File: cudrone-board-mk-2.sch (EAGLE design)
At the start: 170 parts, among them U1 EDISON_CONNECTOR_FULLMOUNTING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, U10 A2235-H, U11 FTS31XS-U, U12 BNO055, U13 DSPIC33EP512MU810-X_PF, U2 FTS31XS-U, U4 TPS62065, U5 USD-SOCKETNEW, U6 TXB0108, U8 PCA9306, U9 PCA9306

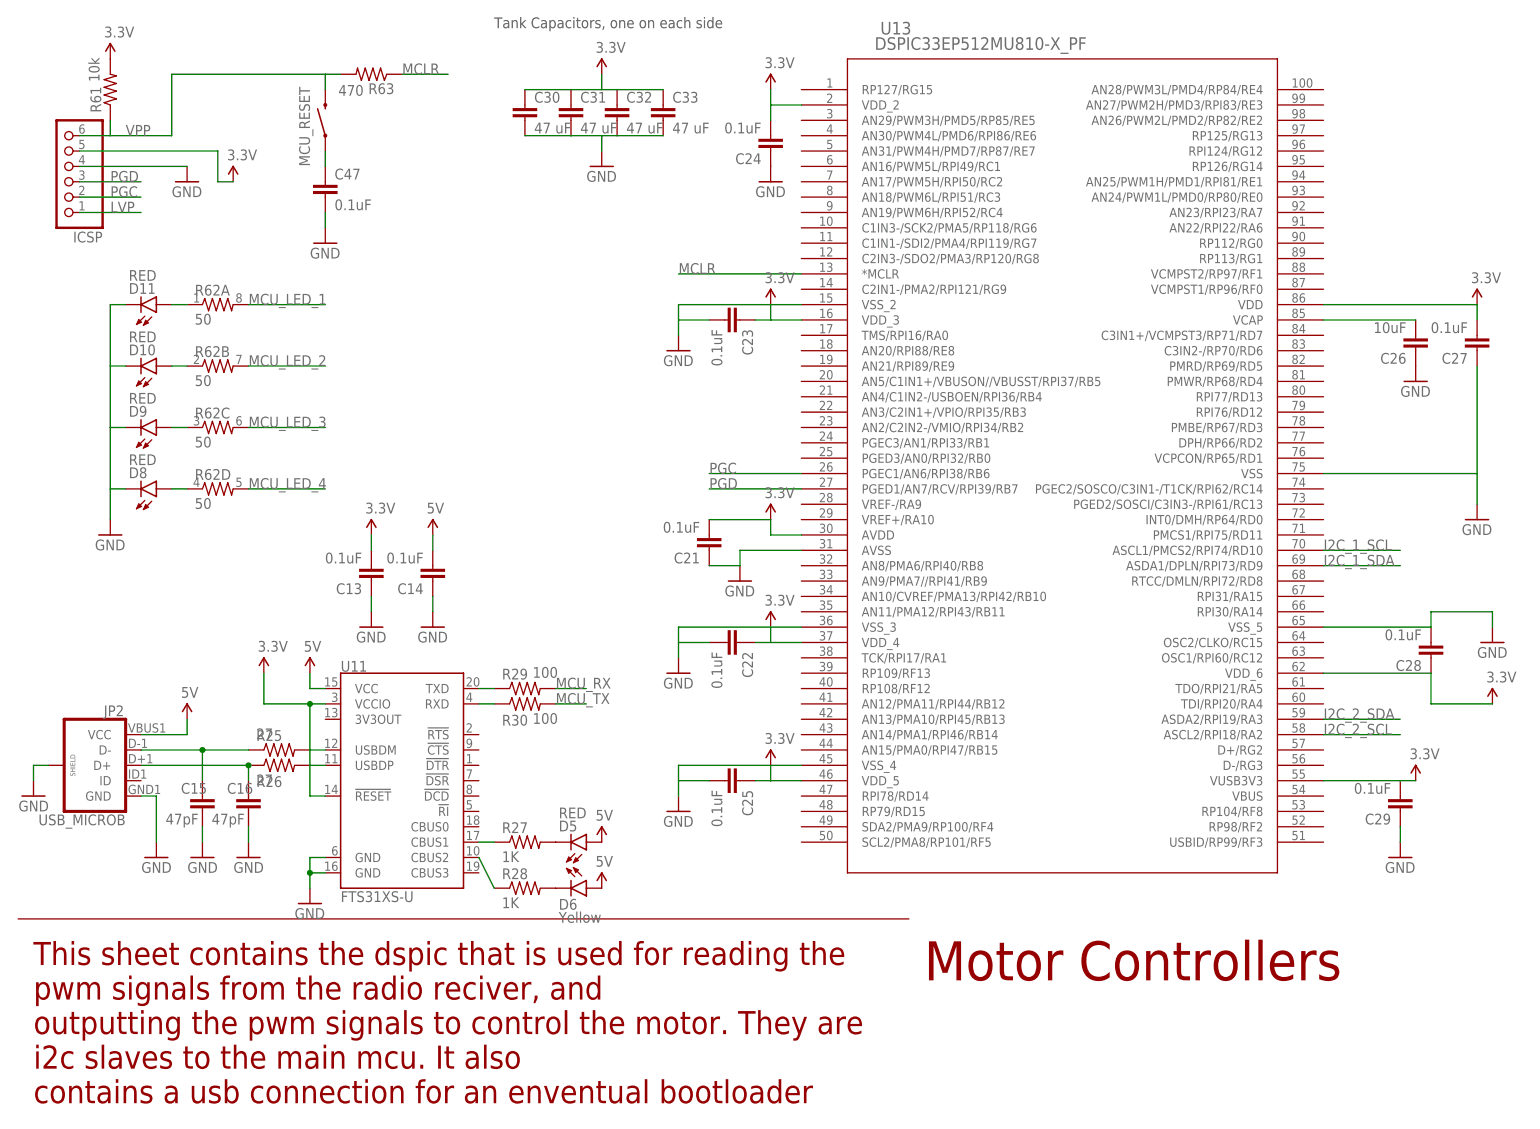
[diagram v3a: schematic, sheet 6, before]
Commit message: Added resinator to mcu
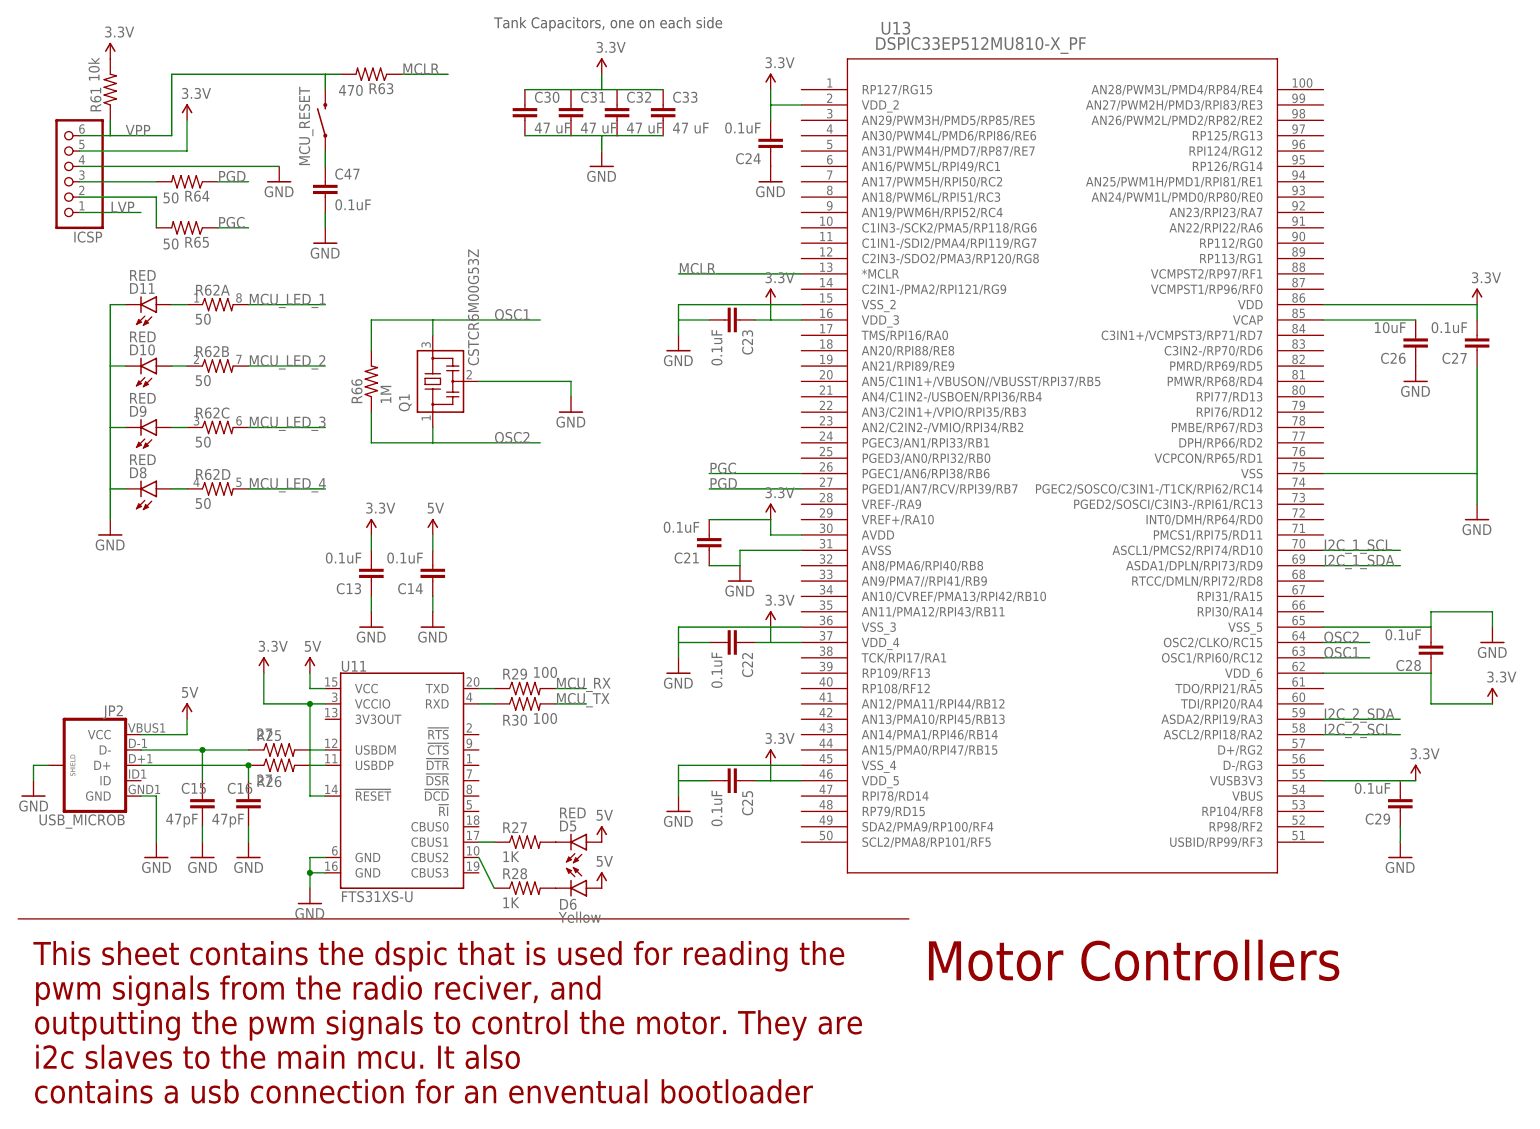
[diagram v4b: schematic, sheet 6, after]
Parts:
- added Q1: CSTCR6M00G53Z, murata-filter:CSTCR6M00G53Z
- added R64, R65: 50, SparkFun-Resistors:27OHM1/10W1%(0603)
- added R66: 1M, SparkFun-Resistors:27OHM1/10W1%(0603)
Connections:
- new net N$46: ICSP.3, R64.2
- new net N$47: ICSP.2, R65.2
- new net OSC1: Q1.3, R66.2, U13.OSC1/RPI60/RC12
- new net OSC2: Q1.1, R66.1, U13.OSC2/CLKO/RC15
- net GND: now also Q1.2
- net PGC: now also R65.1; no longer ICSP.2
- net PGD: now also R64.1; no longer ICSP.3
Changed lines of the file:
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@@
 <part name="MCU_RESET" library="SparkFun-Electromechanical" deviceset="SWITCH-MOMENTARY-2" device=""/>
 <part name="GND83" library="SparkFun-Aesthetics" deviceset="GND" device=""/>
+<part name="R64" library="SparkFun-Resistors" deviceset="27OHM1/10W1%(0603)" device="" value="50"/>
+<part name="R65" library="SparkFun-Resistors" deviceset="27OHM1/10W1%(0603)" device="" value="50"/>
+<part name="Q1" library="murata-filter" deviceset="CSTCR" device="" technology="6M00G53Z"/>
+<part name="GND84" library="SparkFun-Aesthetics" deviceset="GND" device=""/>
+<part name="R66" library="SparkFun-Resistors" deviceset="27OHM1/10W1%(0603)" device="" value="1M"/>
 </parts>
 <sheets>
@@
 <instance part="GND56" gate="1" x="109.22" y="129.54"/>
 <instance part="ICSP" gate="A" x="7.62" y="160.02" rot="R180"/>
-<instance part="GND57" gate="1" x="27.94" y="157.48"/>
-<instance part="SUPPLY100" gate="G$1" x="35.56" y="157.48"/>
+<instance part="GND57" gate="1" x="43.18" y="157.48"/>
+<instance part="SUPPLY100" gate="G$1" x="27.94" y="167.64"/>
 <instance part="R61" gate="G$1" x="15.24" y="172.72" smashed="yes" rot="R90">
 <attribute name="NAME" x="13.7414" y="168.91" size="1.778" layer="95" rot="R90"/>
@@
 </instance>
 <instance part="GND83" gate="1" x="50.8" y="147.32"/>
+<instance part="R64" gate="G$1" x="27.94" y="157.48" smashed="yes" rot="R180">
+<attribute name="NAME" x="31.75" y="155.9814" size="1.778" layer="95" rot="R180"/>
+<attribute name="VALUE" x="26.67" y="155.702" size="1.778" layer="96" rot="R180"/>
+</instance>
+<instance part="R65" gate="G$1" x="27.94" y="149.86" smashed="yes" rot="R180">
+<attribute name="NAME" x="31.75" y="148.3614" size="1.778" layer="95" rot="R180"/>
+<attribute name="VALUE" x="26.67" y="148.082" size="1.778" layer="96" rot="R180"/>
+</instance>
+<instance part="Q1" gate="G$1" x="68.58" y="124.46" rot="R90"/>
+<instance part="GND84" gate="1" x="91.44" y="119.38"/>
+<instance part="R66" gate="G$1" x="58.42" y="124.46" smashed="yes" rot="R90">
+<attribute name="NAME" x="56.9214" y="120.65" size="1.778" layer="95" rot="R90"/>
+<attribute name="VALUE" x="61.722" y="120.65" size="1.778" layer="96" rot="R90"/>
+</instance>
 </instances>
 <busses>
@@
 <pinref part="ICSP" gate="A" pin="4"/>
 <pinref part="GND57" gate="1" pin="GND"/>
-<wire x1="10.16" y1="160.02" x2="27.94" y2="160.02" width="0.1524" layer="91"/>
+<wire x1="10.16" y1="160.02" x2="43.18" y2="160.02" width="0.1524" layer="91"/>
 </segment>
 <segment>
@@
 <wire x1="50.8" y1="149.86" x2="50.8" y2="152.4" width="0.1524" layer="91"/>
 </segment>
+<segment>
+<pinref part="Q1" gate="G$1" pin="2"/>
+<wire x1="76.2" y1="124.46" x2="91.44" y2="124.46" width="0.1524" layer="91"/>
+<pinref part="GND84" gate="1" pin="GND"/>
+<wire x1="91.44" y1="124.46" x2="91.44" y2="121.92" width="0.1524" layer="91"/>
+</segment>
 </net>
 <net name="5V" class="0">
@@
 <segment>
 <pinref part="ICSP" gate="A" pin="5"/>
-<wire x1="10.16" y1="162.56" x2="33.02" y2="162.56" width="0.1524" layer="91"/>
-<wire x1="33.02" y1="162.56" x2="33.02" y2="157.48" width="0.1524" layer="91"/>
 <pinref part="SUPPLY100" gate="G$1" pin="3.3V"/>
-<wire x1="33.02" y1="157.48" x2="35.56" y2="157.48" width="0.1524" layer="91"/>
+<wire x1="10.16" y1="162.56" x2="27.94" y2="162.56" width="0.1524" layer="91"/>
+<wire x1="27.94" y1="162.56" x2="27.94" y2="167.64" width="0.1524" layer="91"/>
 </segment>
 </net>
@@
 <net name="PGD" class="0">
 <segment>
-<pinref part="ICSP" gate="A" pin="3"/>
-<wire x1="10.16" y1="157.48" x2="20.32" y2="157.48" width="0.1524" layer="91"/>
-<label x="15.24" y="157.48" size="1.778" layer="95"/>
-</segment>
-<segment>
 <pinref part="U13" gate="A" pin="PGED1/AN7/RCV/RPI39/RB7"/>
 <wire x1="129.54" y1="106.68" x2="114.3" y2="106.68" width="0.1524" layer="91"/>
 <label x="114.3" y="106.68" size="1.778" layer="95"/>
 </segment>
+<segment>
+<pinref part="R64" gate="G$1" pin="1"/>
+<wire x1="33.02" y1="157.48" x2="38.1" y2="157.48" width="0.1524" layer="91"/>
+<label x="33.02" y="157.48" size="1.778" layer="95"/>
+</segment>
 </net>
 <net name="PGC" class="0">
-<segment>
-<pinref part="ICSP" gate="A" pin="2"/>
-<wire x1="10.16" y1="154.94" x2="20.32" y2="154.94" width="0.1524" layer="91"/>
-<label x="15.24" y="154.94" size="1.778" layer="95"/>
-</segment>
 <segment>
 <pinref part="U13" gate="A" pin="PGEC1/AN6/RPI38/RB6"/>
@@
 <label x="114.3" y="109.22" size="1.778" layer="95"/>
 </segment>
+<segment>
+<pinref part="R65" gate="G$1" pin="1"/>
+<wire x1="33.02" y1="149.86" x2="38.1" y2="149.86" width="0.1524" layer="91"/>
+<label x="33.02" y="149.86" size="1.778" layer="95"/>
+</segment>
 </net>
 <net name="LVP" class="0">
@@
 </segment>
 </net>
+<net name="N$46" class="0">
+<segment>
+<pinref part="ICSP" gate="A" pin="3"/>
+<pinref part="R64" gate="G$1" pin="2"/>
+<wire x1="10.16" y1="157.48" x2="22.86" y2="157.48" width="0.1524" layer="91"/>
+</segment>
+</net>
+<net name="N$47" class="0">
+<segment>
+<pinref part="ICSP" gate="A" pin="2"/>
+<pinref part="R65" gate="G$1" pin="2"/>
+<wire x1="10.16" y1="154.94" x2="22.86" y2="154.94" width="0.1524" layer="91"/>
+<wire x1="22.86" y1="154.94" x2="22.86" y2="149.86" width="0.1524" layer="91"/>
+</segment>
+</net>
+<net name="OSC2" class="0">
+<segment>
+<pinref part="U13" gate="A" pin="OSC2/CLKO/RC15"/>
+<wire x1="215.9" y1="81.28" x2="223.52" y2="81.28" width="0.1524" layer="91"/>
+<label x="215.9" y="81.28" size="1.778" layer="95"/>
+</segment>
+<segment>
+<pinref part="Q1" gate="G$1" pin="1"/>
+<wire x1="68.58" y1="116.84" x2="68.58" y2="114.3" width="0.1524" layer="91"/>
+<wire x1="68.58" y1="114.3" x2="86.36" y2="114.3" width="0.1524" layer="91"/>
+<label x="78.74" y="114.3" size="1.778" layer="95"/>
+<pinref part="R66" gate="G$1" pin="1"/>
+<wire x1="58.42" y1="119.38" x2="58.42" y2="114.3" width="0.1524" layer="91"/>
+<wire x1="58.42" y1="114.3" x2="68.58" y2="114.3" width="0.1524" layer="91"/>
+</segment>
+</net>
+<net name="OSC1" class="0">
+<segment>
+<pinref part="U13" gate="A" pin="OSC1/RPI60/RC12"/>
+<wire x1="215.9" y1="78.74" x2="223.52" y2="78.74" width="0.1524" layer="91"/>
+<label x="215.9" y="78.74" size="1.778" layer="95"/>
+</segment>
+<segment>
+<pinref part="Q1" gate="G$1" pin="3"/>
+<wire x1="68.58" y1="132.08" x2="68.58" y2="134.62" width="0.1524" layer="91"/>
+<wire x1="68.58" y1="134.62" x2="86.36" y2="134.62" width="0.1524" layer="91"/>
+<label x="78.74" y="134.62" size="1.778" layer="95"/>
+<pinref part="R66" gate="G$1" pin="2"/>
+<wire x1="58.42" y1="129.54" x2="58.42" y2="134.62" width="0.1524" layer="91"/>
+<wire x1="58.42" y1="134.62" x2="68.58" y2="134.62" width="0.1524" layer="91"/>
+</segment>
+</net>

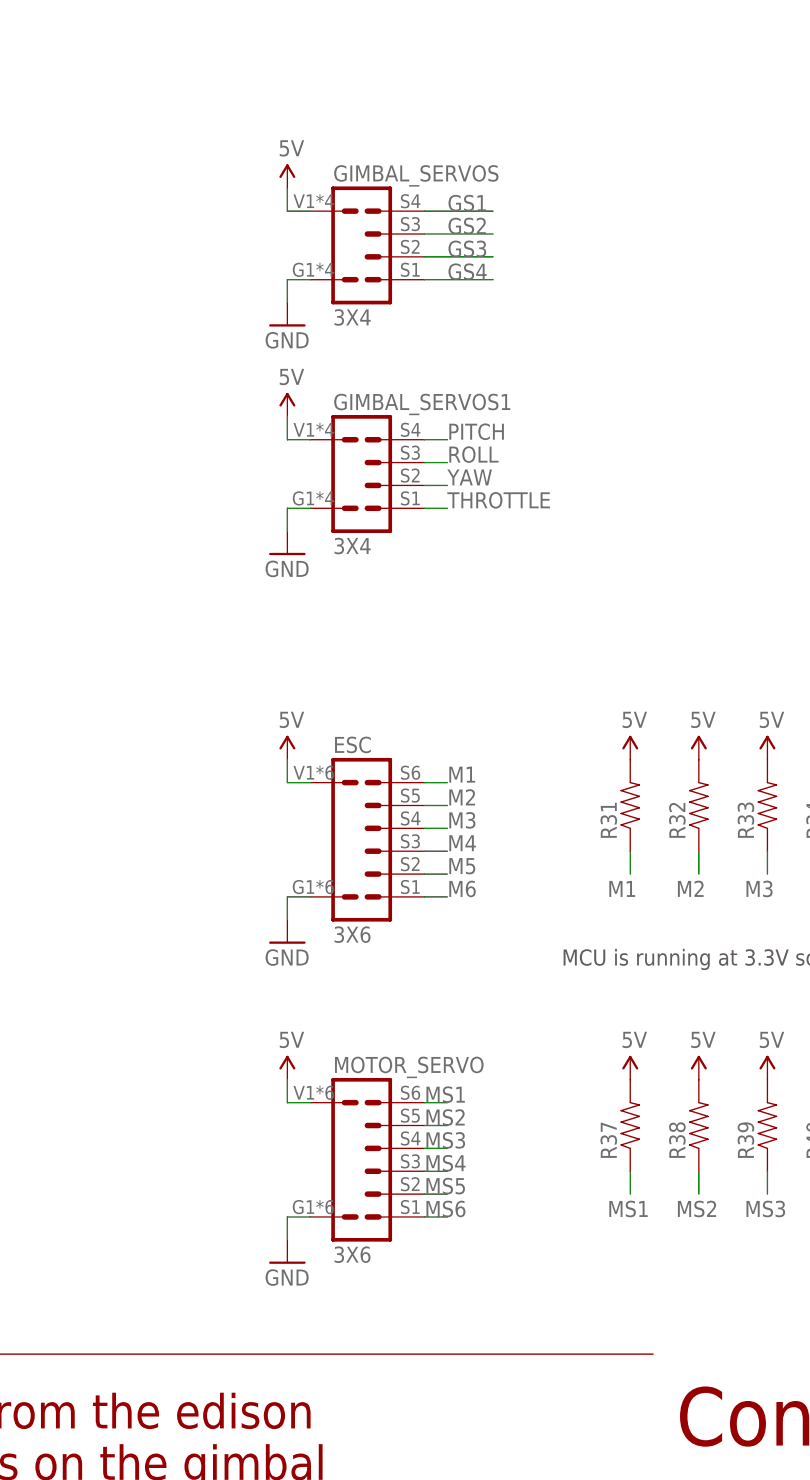
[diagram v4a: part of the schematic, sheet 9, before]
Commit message: Added longer pin headers for servos and connected io to mcu
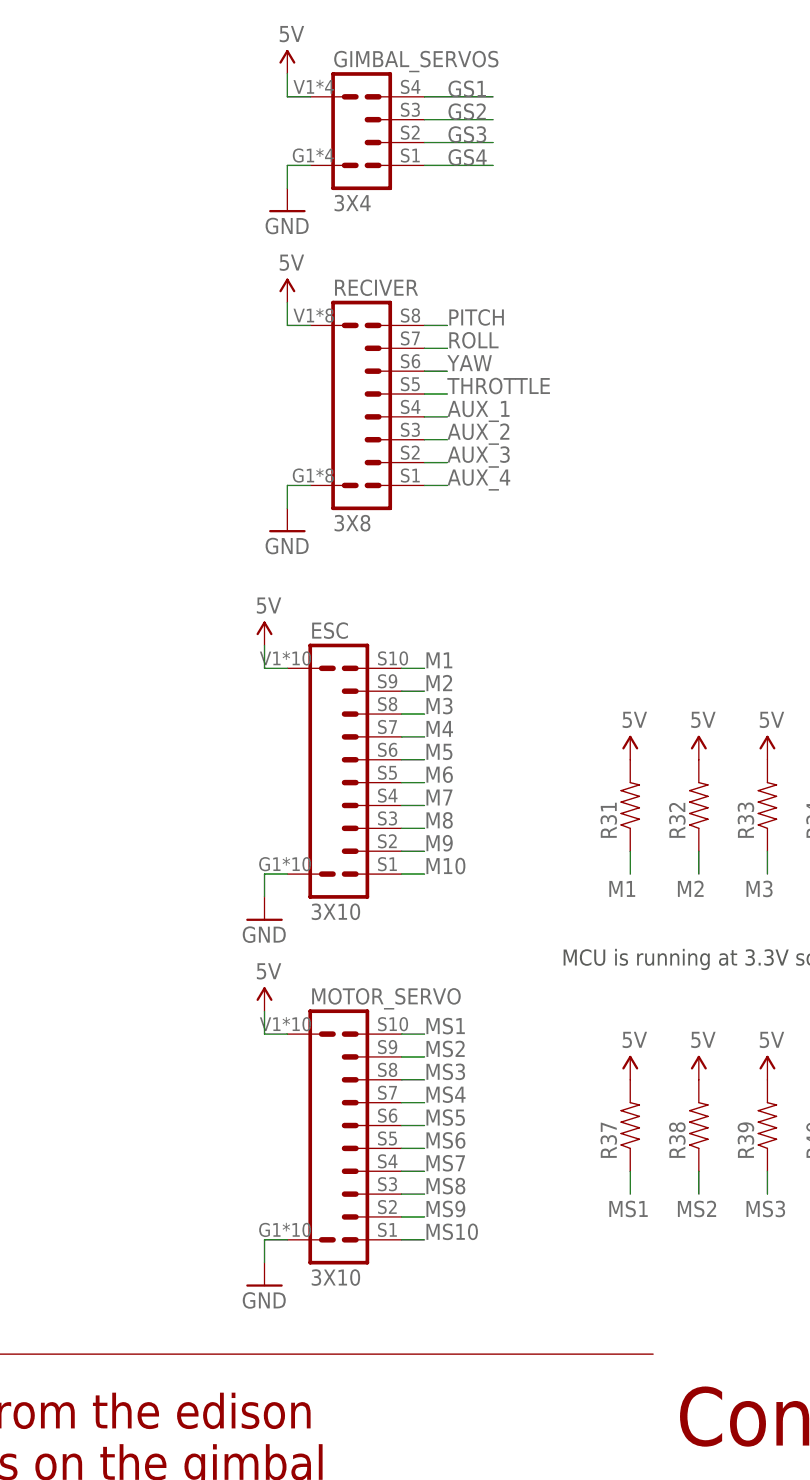
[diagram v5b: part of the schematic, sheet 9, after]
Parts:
- removed GIMBAL_SERVOS1: 3X4, Drone_Connectors:3X4
- removed JP4: (no value), SparkFun-Connectors:M03PTH
- added RECIVER: 3X8, Drone_Connectors:3X8
- ESC, MOTOR_SERVO: value 3X6 -> 3X10; device Drone_Connectors:3X6 -> Drone_Connectors:3X10
- JP3: device SparkFun-Connectors:M03PTH -> SparkFun-Connectors:M03X2DOUBLE_JUMPER_SWAP
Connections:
- new net AUX_1: RECIVER.4, U13.AN12/PMA11/RPI44/RB12
- new net AUX_2: RECIVER.3, U13.AN13/PMA10/RPI45/RB13
- new net AUX_3: RECIVER.2, U13.AN14/PMA1/RPI46/RB14
- new net AUX_4: RECIVER.1, U13.AN15/PMA0/RPI47/RB15
- new net M10: ESC.1, U13.RP98/RF2
- new net M7: ESC.4, U13.DPH/RP66/RD2
- new net M8: ESC.3, U13.VCPCON/RP65/RD1
- new net M9: ESC.2, U13.RP104/RF8
- new net MS10: MOTOR_SERVO.1, U13.PMBE/RP67/RD3
- new net MS7: MOTOR_SERVO.4, U13.C1IN3-/SCK2/PMA5/RP118/RG6
- new net MS8: MOTOR_SERVO.3, U13.SDA2/PMA9/RP100/RF4
- new net MS9: MOTOR_SERVO.2, U13.SCL2/PMA8/RP101/RF5
- net 5V: now also RECIVER.V; no longer GIMBAL_SERVOS1.V
- net CON_RX: now also JP3.1; no longer JP4.1
- net CON_TX: now also JP3.2; no longer JP3.1
- net GND: now also RECIVER.G; no longer GIMBAL_SERVOS1.G
- net GP134_UART_2_RX: now also JP3.4; no longer JP3.2
- net GP135_UART_2_TX: now also JP3.3; no longer JP4.2
- net M1: now also ESC.10, U13.AN28/PWM3L/PMD4/RP84/RE4; no longer ESC.8
- net M2: now also ESC.9, U13.AN26/PWM2L/PMD2/RP82/RE2; no longer ESC.7
- net M3: now also ESC.8, U13.AN24/PWM1L/PMD0/RP80/RE0; no longer ESC.6
- net M4: now also ESC.7, U13.AN29/PWM3H/PMD5/RP85/RE5; no longer ESC.5
- net M5: now also ESC.6, U13.AN31/PWM4H/PMD7/RP87/RE7; no longer ESC.4
- net M6: now also ESC.5, U13.AN30/PWM4L/PMD6/RPI86/RE6; no longer ESC.3
- net MS1: now also MOTOR_SERVO.10, U13.AN27/PWM2H/PMD3/RPI83/RE3; no longer MOTOR_SERVO.8
- net MS2: now also MOTOR_SERVO.9, U13.AN25/PWM1H/PMD1/RPI81/RE1; no longer MOTOR_SERVO.7
- net MS3: now also MOTOR_SERVO.8, U13.AN16/PWM5L/RPI49/RC1; no longer MOTOR_SERVO.6
- net MS4: now also MOTOR_SERVO.7, U13.AN17/PWM5H/RPI50/RC2; no longer MOTOR_SERVO.5
- net MS5: now also MOTOR_SERVO.6, U13.AN18/PWM6L/RPI51/RC3; no longer MOTOR_SERVO.4
- net MS6: now also MOTOR_SERVO.5, U13.AN19/PWM6H/RPI52/RC4; no longer MOTOR_SERVO.3
- net PITCH: now also RECIVER.8, U13.C1IN1-/SDI2/PMA4/RPI119/RG7; no longer GIMBAL_SERVOS1.S4
- net ROLL: now also RECIVER.7, U13.C2IN3-/SDO2/PMA3/RP120/RG8; no longer GIMBAL_SERVOS1.S3
- net THROTTLE: now also RECIVER.5, U13.PGED3/AN0/RPI32/RB0; no longer GIMBAL_SERVOS1.S1
- net XBEE_RX_LOW: now also JP3.5; no longer JP4.3
- net XBEE_TX_LOW: now also JP3.6; no longer JP3.3
- net YAW: now also RECIVER.6, U13.PGEC3/AN1/RPI33/RB1; no longer GIMBAL_SERVOS1.S2
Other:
- moved on the sheet: C21, C24, C25, C29, C30, C31, C32, C33, GIMBAL_SERVOS
